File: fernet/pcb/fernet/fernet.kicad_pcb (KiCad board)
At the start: 2 copper layers, 320.5 x 127.5 mm, 165 parts, among them SW0 Rotary_Encoder_Switch, SW1 Rotary_Encoder_Switch, SW2 Rotary_Encoder_Switch, U0 Elite-C

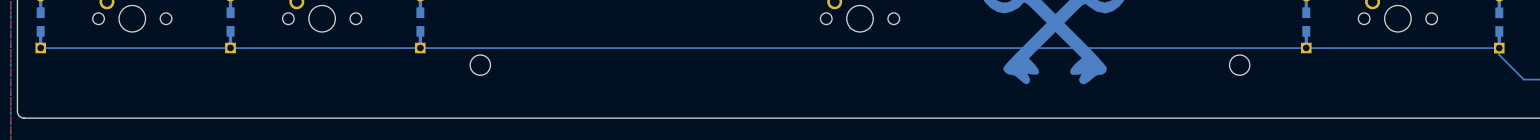
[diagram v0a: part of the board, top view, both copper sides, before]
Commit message: Update fernet PCB to fix exposed trace
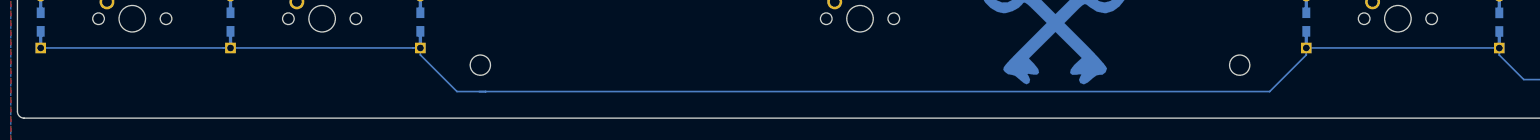
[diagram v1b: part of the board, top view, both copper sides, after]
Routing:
- net row5: track 404.6 -> 412.3 mm
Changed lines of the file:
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@@
     (thickness 1.6)
     (drawings 13)
-    (tracks 749)
+    (tracks 761)
     (zones 0)
     (modules 165)
@@
   (segment (start 272.9125 138.7) (end 243.7447 138.7) (width 0.25) (layer B.Cu) (net 28))
   (segment (start 20.51812 133.95562) (end 20.5 133.9375) (width 0.25) (layer B.Cu) (net 28))
-  (segment (start 240.05032 133.95562) (end 20.51812 133.95562) (width 0.25) (layer B.Cu) (net 28))
   (via (at 328.653699 48) (size 0.8) (drill 0.4) (layers F.Cu B.Cu) (net 28))
   (segment (start 328.653699 45.137026) (end 328.653699 48) (width 0.25) (layer B.Cu) (net 28))
@@
   (segment (start 313 136) (end 311.1125 136) (width 0.25) (layer B.Cu) (net 28))
   (segment (start 333.12 41.91) (end 334.898 41.91) (width 0.25) (layer B.Cu) (net 28))
+  (segment (start 211 134.9875) (end 205.4875 140.5) (width 0.25) (layer B.Cu) (net 28))
+  (segment (start 211 133.9375) (end 211 134.9875) (width 0.25) (layer B.Cu) (net 28))
+  (segment (start 77.65 134.9875) (end 83.1625 140.5) (width 0.25) (layer B.Cu) (net 28))
+  (segment (start 77.65 133.9375) (end 77.65 134.9875) (width 0.25) (layer B.Cu) (net 28))
+  (segment (start 83.1625 140.5) (end 87.5 140.5) (width 0.25) (layer B.Cu) (net 28))
+  (segment (start 205.4875 140.5) (end 87.5 140.5) (width 0.25) (layer B.Cu) (net 28))
+  (segment (start 87.5 140.5) (end 86.5 140.5) (width 0.25) (layer B.Cu) (net 28))
+  (segment (start 76.6 133.9375) (end 49.075 133.9375) (width 0.25) (layer B.Cu) (net 28))
+  (segment (start 77.65 133.9375) (end 76.6 133.9375) (width 0.25) (layer B.Cu) (net 28))
+  (segment (start 48.025 133.9375) (end 20.5 133.9375) (width 0.25) (layer B.Cu) (net 28))
+  (segment (start 49.075 133.9375) (end 48.025 133.9375) (width 0.25) (layer B.Cu) (net 28))
+  (segment (start 240.0322 133.9375) (end 240.05032 133.95562) (width 0.25) (layer B.Cu) (net 28))
+  (segment (start 211 133.9375) (end 240.0322 133.9375) (width 0.25) (layer B.Cu) (net 28))
   (segment (start 79.33 124.4575) (end 146.365 124.4575) (width 0.25) (layer B.Cu) (net 29))
   (segment (start 77.65 126.1375) (end 79.33 124.4575) (width 0.25) (layer B.Cu) (net 29))

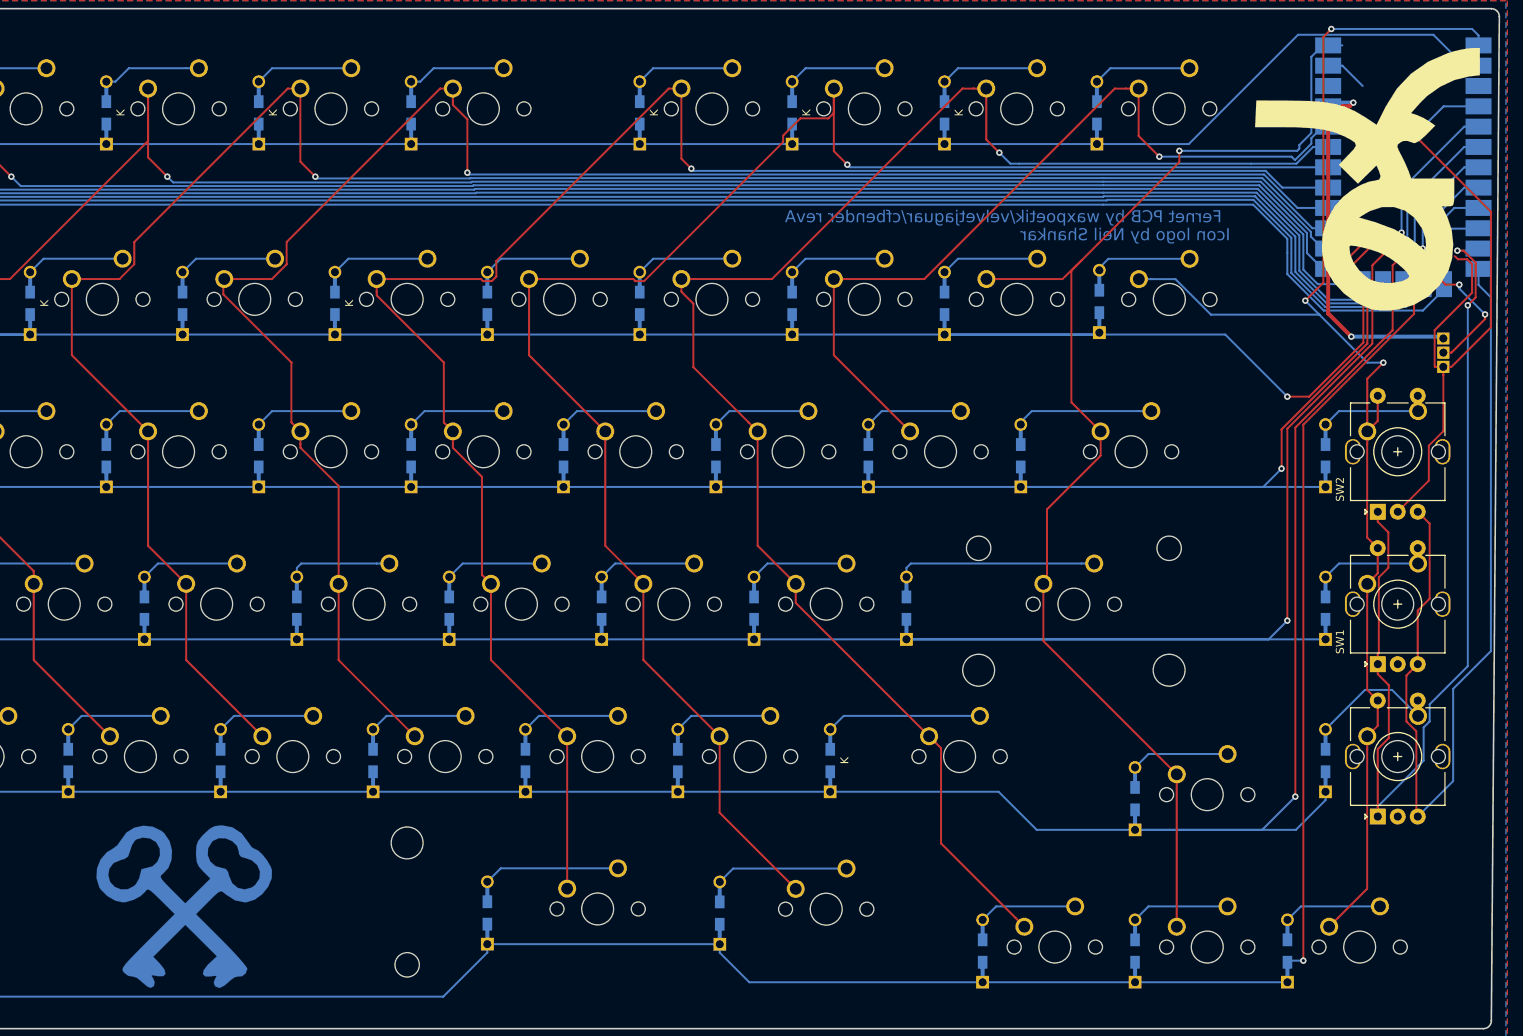
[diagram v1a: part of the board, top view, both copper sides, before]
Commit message: Add 2u backspace support to fernet
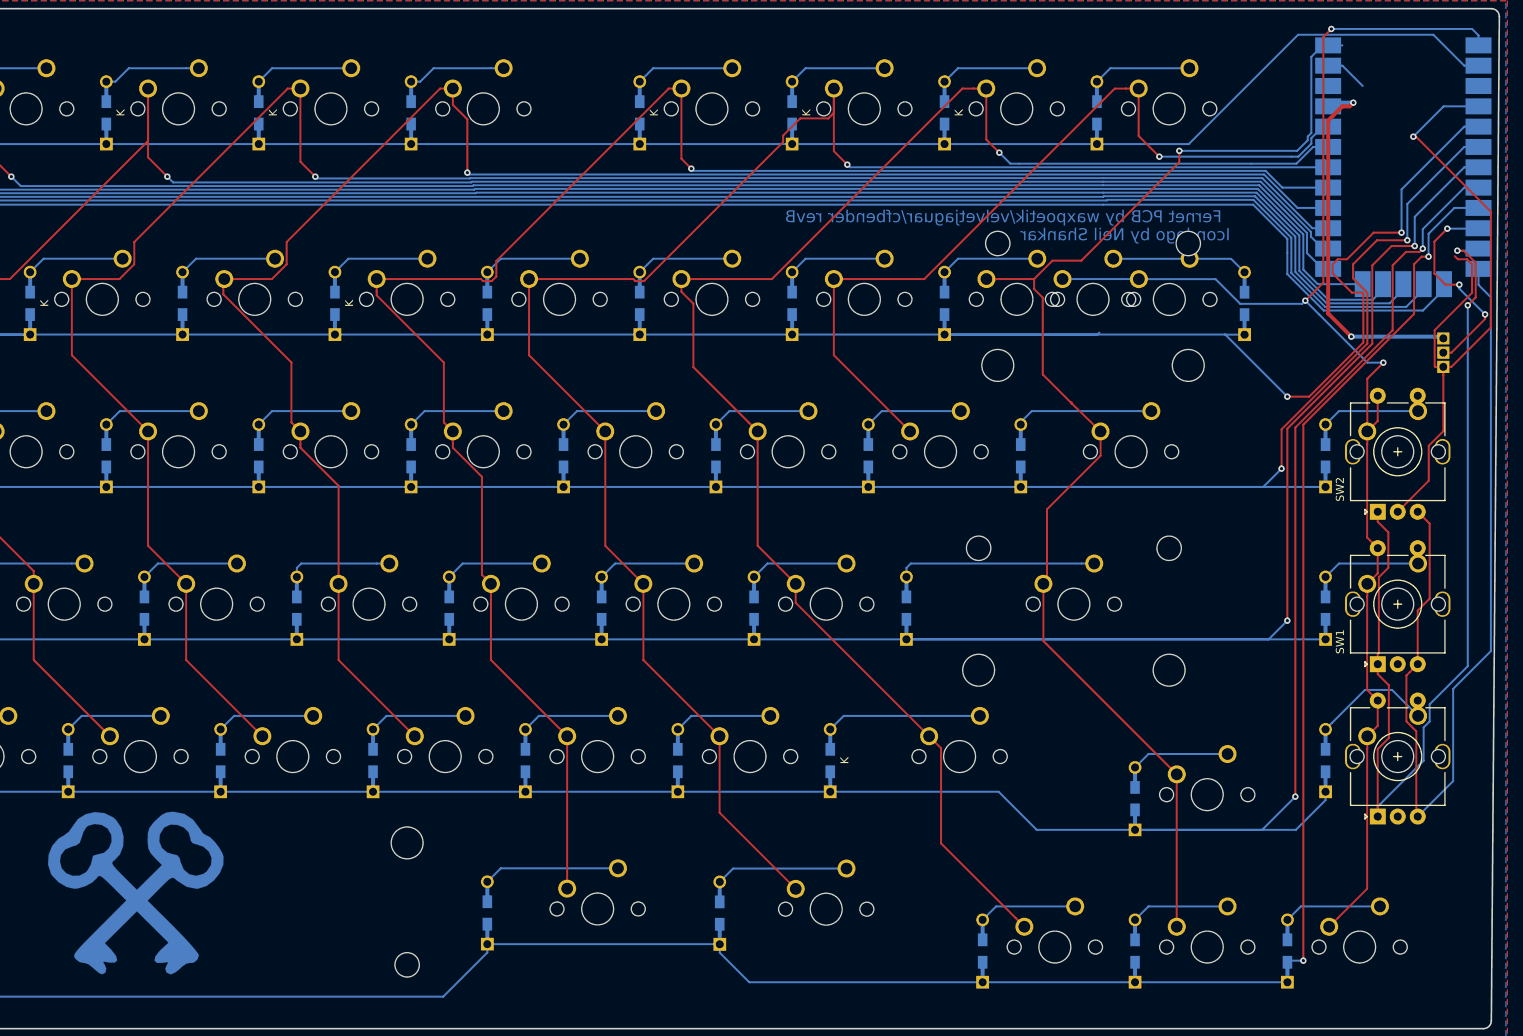
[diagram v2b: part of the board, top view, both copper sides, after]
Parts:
- removed the G*** at (322.5, 38.5)
- added K_BKSPC2: KEYSW, MX_Only:MXOnly-2U-NoLED, F.Cu at (286.7, 53.3)
- moved D_DEL1 18.2 mm to (305.6, 53.9)
- moved G*** 6.10 mm to (167.2, 128.5)
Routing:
- net col14: track 173.2 -> 180.6 mm
- net Net-(D_DEL1-Pad2): track 13.5 -> 17.7 mm
- net row1: track 387.1 -> 389.5 mm
- net col13: track 158.2 -> 157.5 mm
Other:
- board text added: "Fernet PCB by waxpoetik/velvetjaguar/cfbender revB"
- board text removed: "Fernet PCB by waxpoetik/velvetjaguar/cfbender revA"
